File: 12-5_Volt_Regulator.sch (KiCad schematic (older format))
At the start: 21 parts, among them J1 Conn_01x02, J2 Conn_01x02, U1 LM22676MR-5

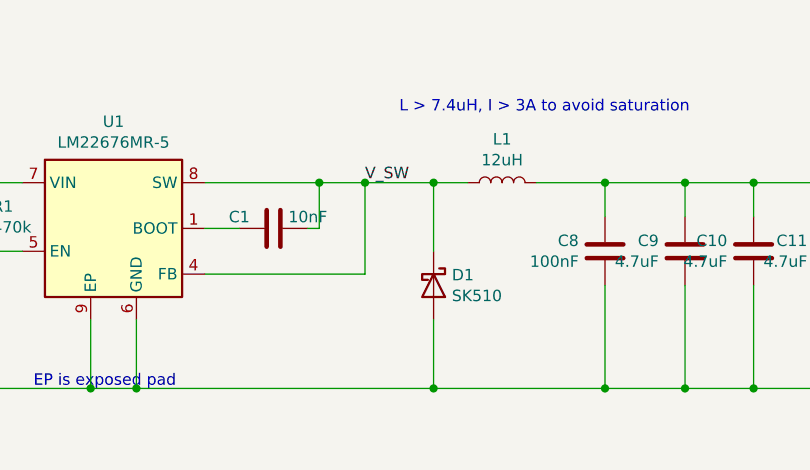
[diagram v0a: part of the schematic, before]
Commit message: Rev 2. Fixed feedback loop, added R3 for EMI suppression
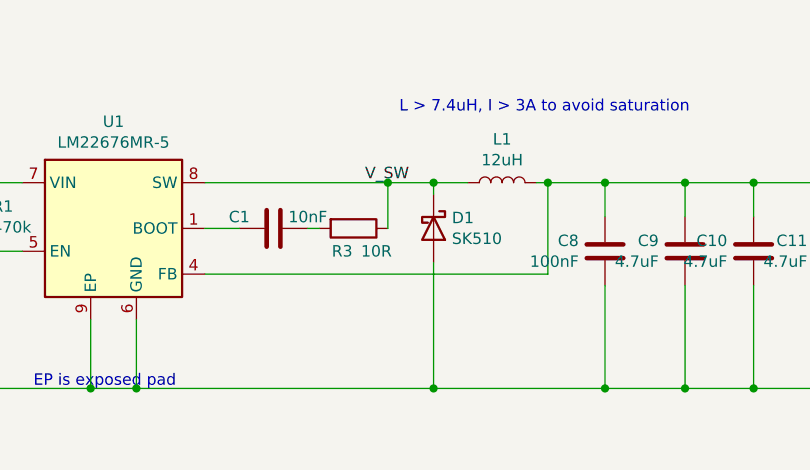
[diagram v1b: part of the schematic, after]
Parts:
- added R3: 10R, Resistor_SMD:R_0603_1608Metric, symbol Device:R
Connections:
- net 5v: now also U1.4 (FB)
- net V_SW: now also R3.1; no longer C1.1, U1.4 (FB)
- new net: C1.1, R3.2
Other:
- moved on the sheet: D1
